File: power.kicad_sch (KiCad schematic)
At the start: 30 parts, among them Q2 BSS138-7-F, Q3 BSS138-7-F, Q7 SQS401EN-T1_BE3, U1 TPS56C230

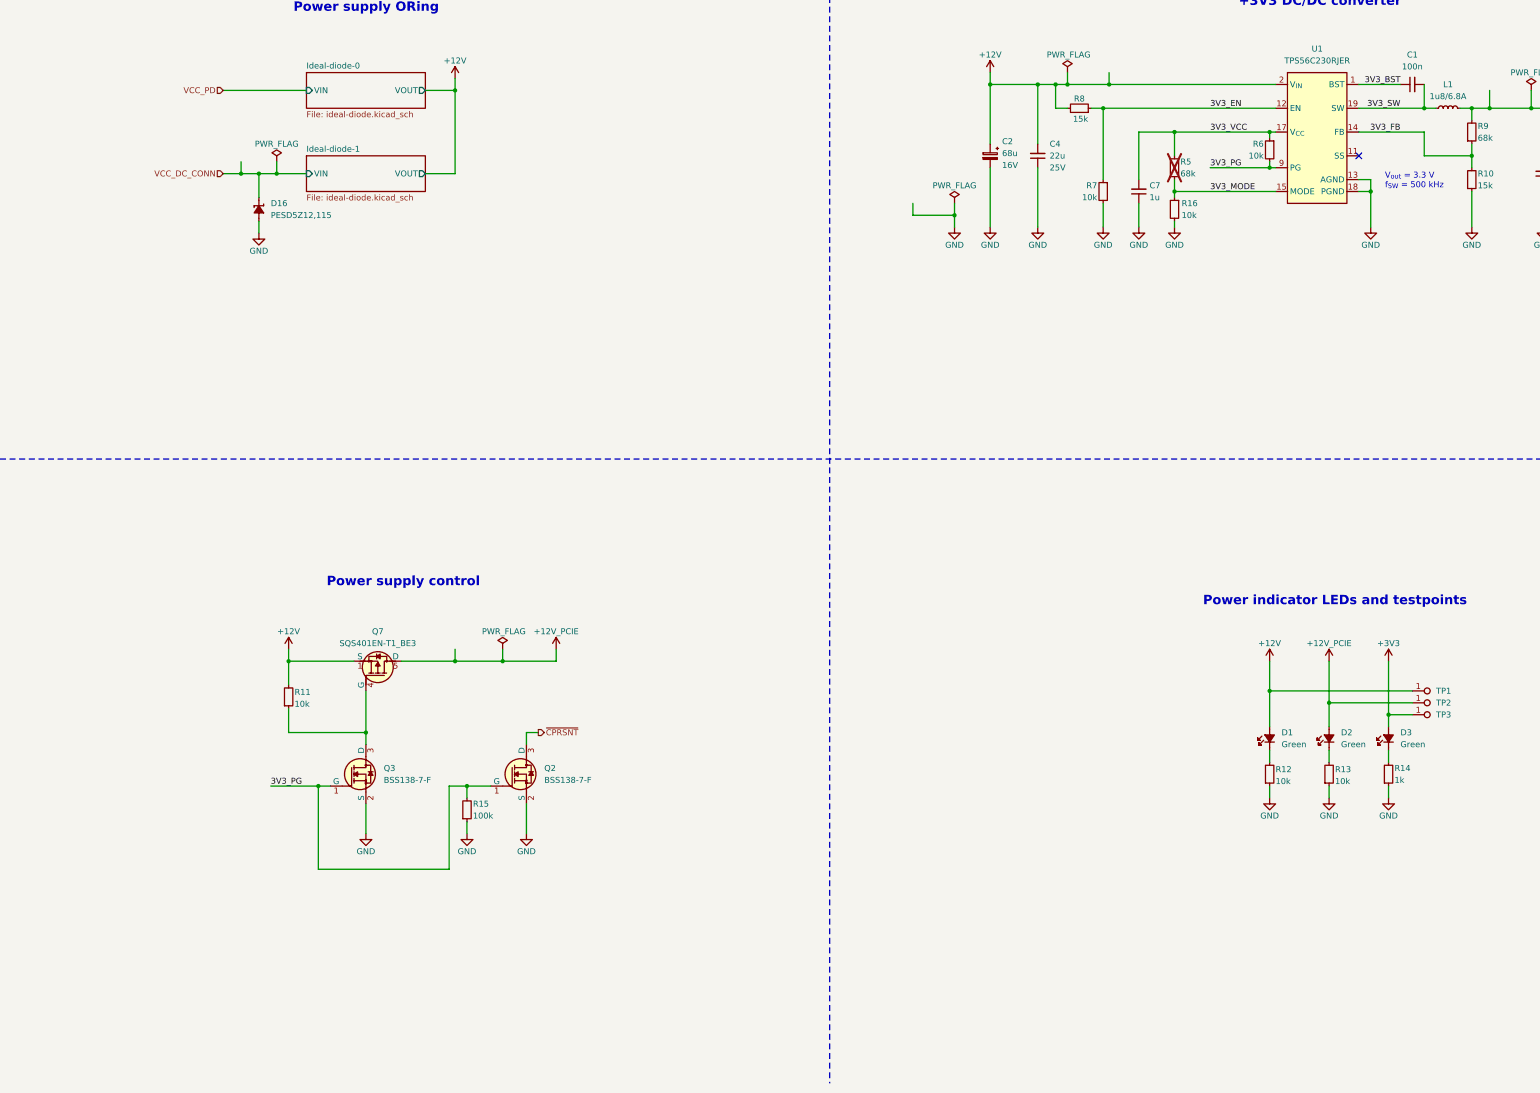
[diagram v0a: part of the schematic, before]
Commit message: [#79426] Removed power sequencing, added PERST control
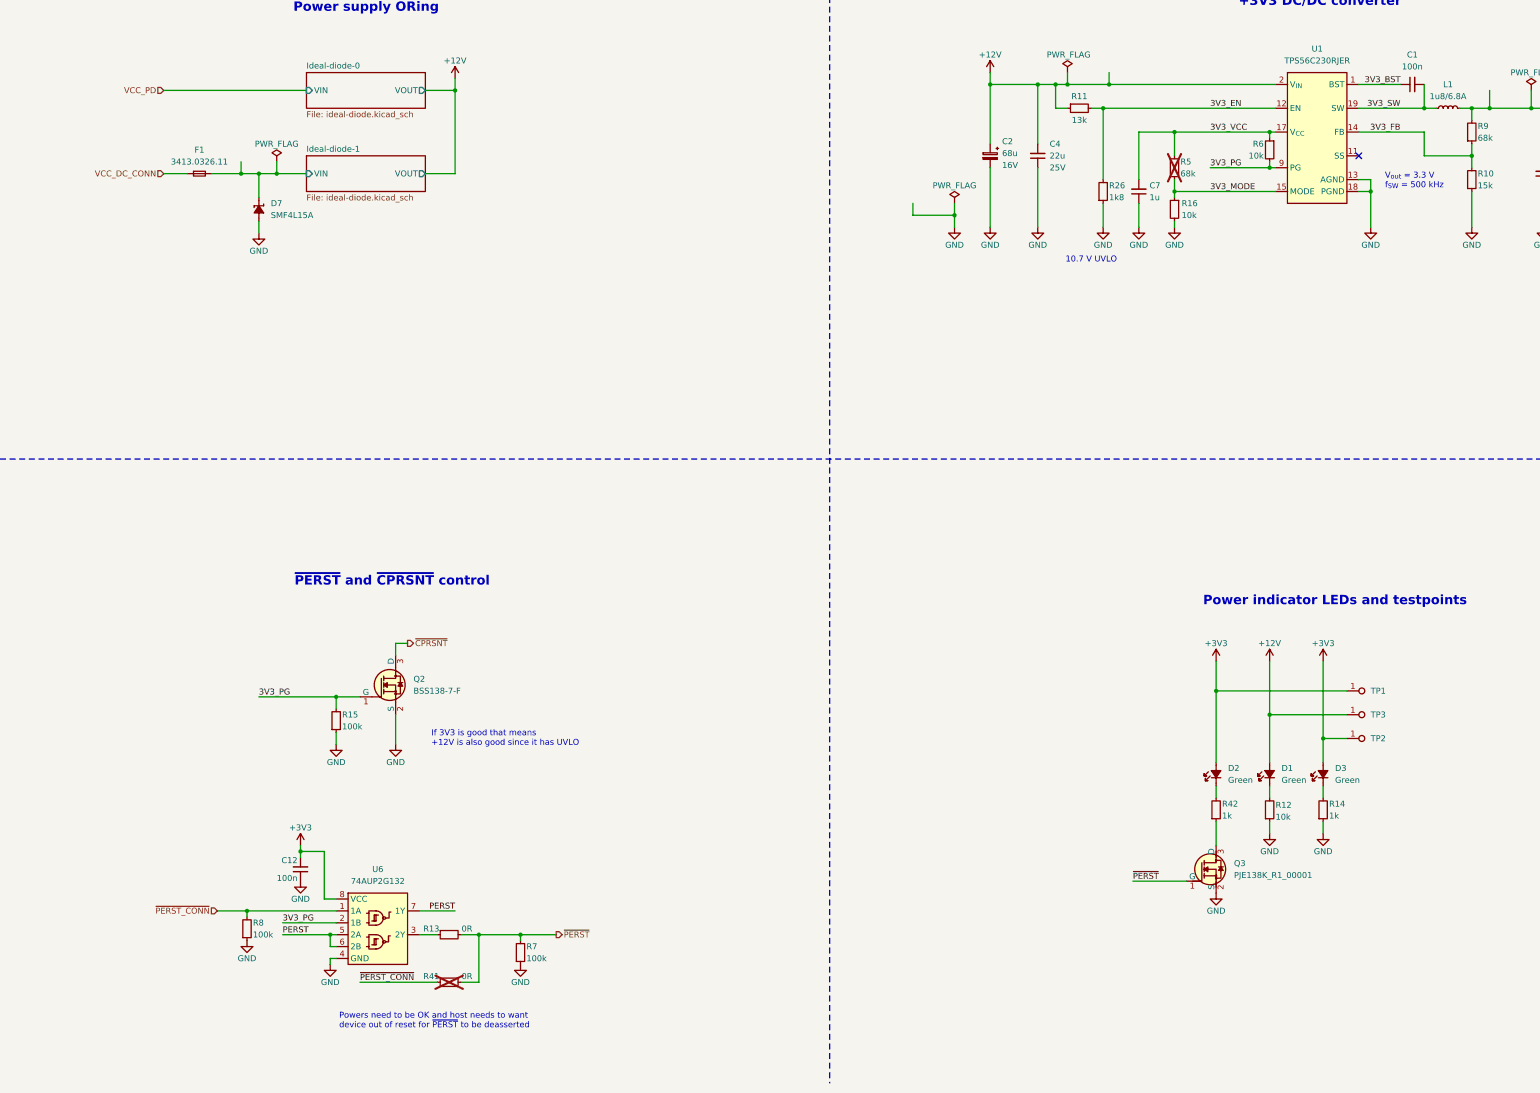
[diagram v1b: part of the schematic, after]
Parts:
- removed D16: PESD5Z12, antmicro-footprints:SOD-523, symbol antmicroTVSDiodes:PESD5Z12
- removed Q3: BSS138-7-F, antmicro-footprints:SOT-23-3, symbol antmicroTransistorsFETsMOSFETsSingle:BSS138-7-F
- removed Q7: SQS401EN-T1_BE3, antmicro-footprints:Vishay_PowerPAK_1212-8_Single, symbol antmicroTransistorsFETsMOSFETsSingle:SQS401EN-T1_BE3
- removed R11, R13, R7: R_10k_0402, antmicro-footprints:R_0402_1005Metric, symbol antmicroResistors0402:R_10k_0402
- removed R8: R_15k_0402, antmicro-footprints:R_0402_1005Metric, symbol antmicroResistors0402:R_15k_0402
- added C12: C_100n_0402, antmicro-footprints:C_0402_1005Metric, symbol antmicroCapacitors0402:C_100n_0402
- added D7: SMF4L15A, antmicro-footprints:SOD-123FL, symbol antmicroTVSDiodes:SMF4L15A
- added F1: F_7A_1206, antmicro-footprints:F_1206_3216Metric, symbol antmicroFuses:F_7A_1206
- added Q3: PJE138K, antmicro-footprints:SOT-523, symbol antmicroTransistorsFETsMOSFETsSingle:PJE138K
- added R11: R_13k_0402, antmicro-footprints:R_0402_1005Metric, symbol antmicroResistors0402:R_13k_0402
- added R13, R41: R_0R_0402, antmicro-footprints:R_0402_1005Metric, symbol antmicroResistors0402:R_0R_0402
- added R26: R_1k8_0603, antmicro-footprints:R_0603_1608Metric, symbol antmicroResistors0603:R_1k8_0603
- added R42: R_1k_0402, antmicro-footprints:R_0402_1005Metric, symbol antmicroResistors0402:R_1k_0402
- added R7, R8: R_100k_0402, antmicro-footprints:R_0402_1005Metric, symbol antmicroResistors0402:R_100k_0402
- added U6: 74AUP2G132, antmicro-footprints:VSSOP-8_2.3x2mm_P0.5mm, symbol antmicroLogicGatesandInverters:74AUP2G132
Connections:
- net +12V_PCIE is gone; now on net +3V3: D2.2 (A), TP2.1
- net +12V: now also TP3.1, R11.1; no longer TP1.1
- net +3V3: now also TP1.1, C12.2, U6.8 (VCC); no longer TP3.1
- net 3V3_EN: now also R11.2, R26.2
- net 3V3_PG: now also U6.2 (1B)
- net GND: now also C12.1, D7.2 (A), Q3.2 (S), R26.1, R7.1, R8.1, U6.4 (GND)
- net VCC_DC_CONN: now also F1.1
- net at D2.1 (C): now also R42.2
- new net: Q3.3 (D), R42.1
- new net: R13.1, U6.3 (2Y)
- new net Ideal-diode-1/VIN: D7.1 (C), F1.2
- new net PERST: U6.5 (2A), U6.6 (2B), U6.7 (1Y)
- new net ~{PERST_CONN}: R41.1, R8.2, U6.1 (1A)
- new net ~{PERST}: Q3.1 (G), R13.2, R41.2, R7.2
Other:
- note added: "10.7 V UVLO"
- note added: "If 3V3 is good that means +12V is also good since it has UVLO"
- note added: "Powers need to be OK and host needs to want device out of reset for ~{PERST} to be deasserted"
- note added: "~{PERST} and ~{CPRSNT} control"
- note removed: "Power supply control"
- moved on the sheet: D1, D3, Q2, R12, R14, R15, TP1, TP3

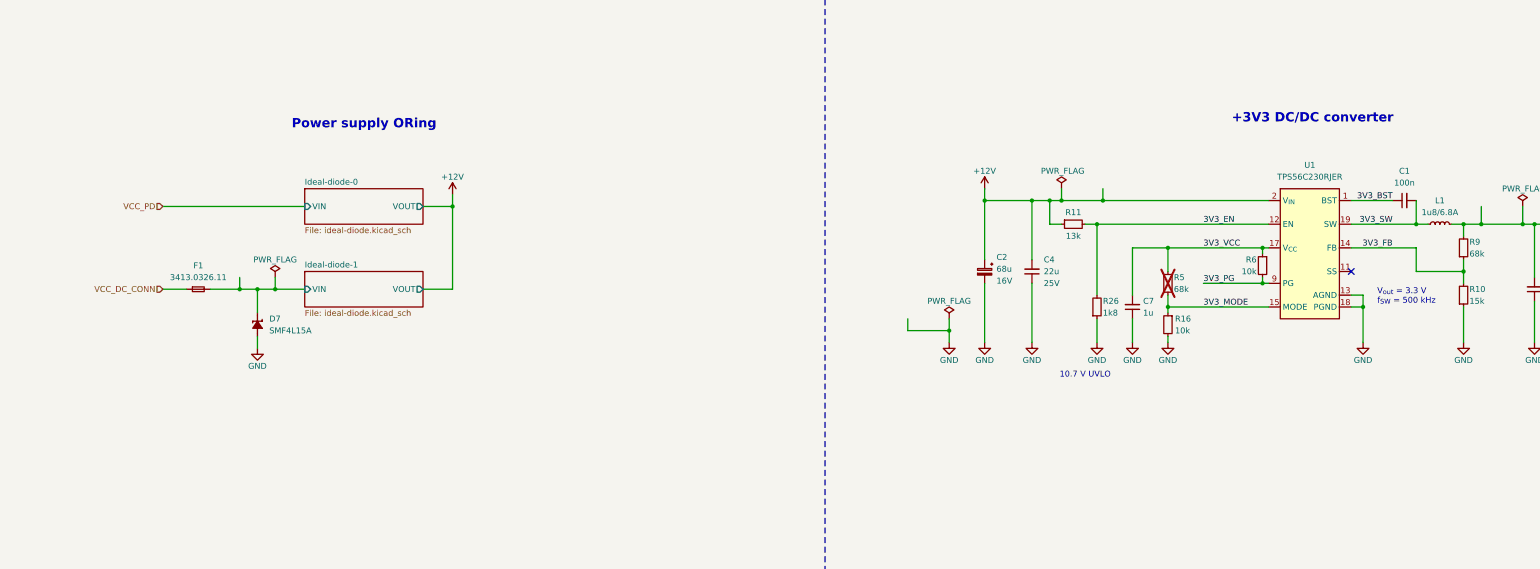
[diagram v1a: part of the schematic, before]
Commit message: [#79426] Connect DC input connectors via ideal diodes, change 15V TVS to 12V TVS
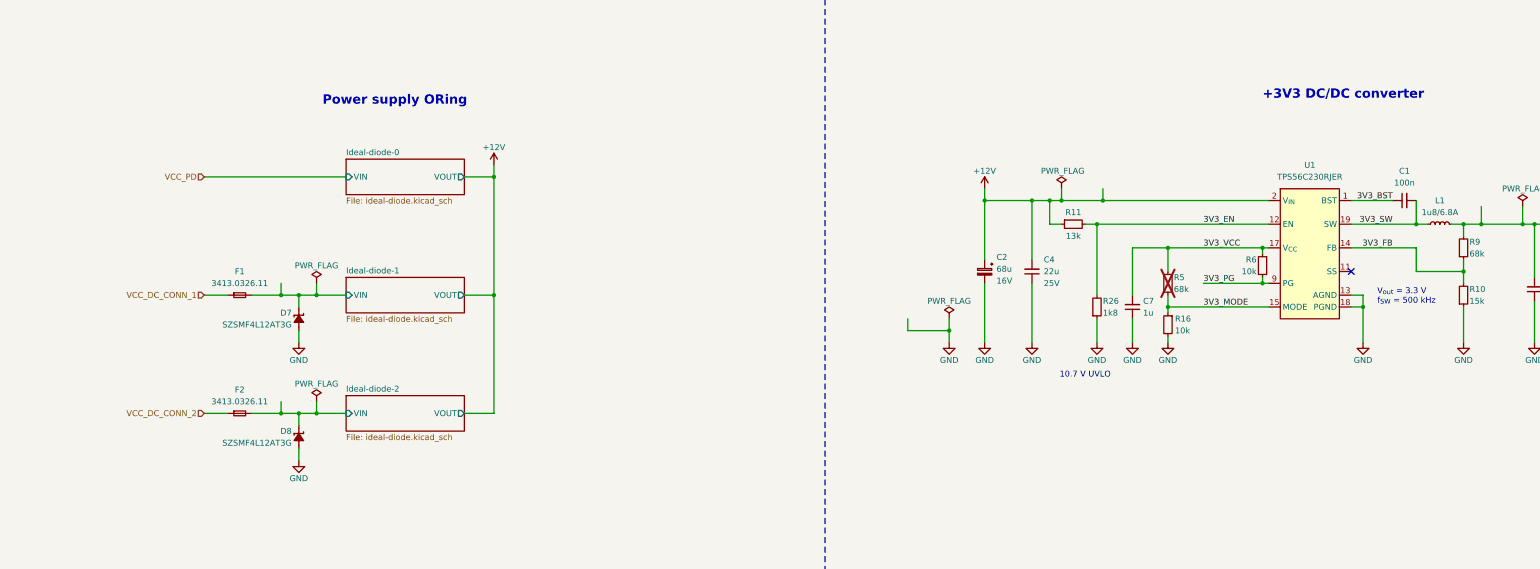
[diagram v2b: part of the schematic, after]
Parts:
- removed D7: SMF4L15A, antmicro-footprints:SOD-123FL, symbol antmicroTVSDiodes:SMF4L15A
- added D7, D8: SZSMF4L14AT3G, antmicro-footprints:SOD-123FL, symbol antmicroTVSDiodes:SZSMF4L14AT3G
- added F2: F_7A_1206, antmicro-footprints:F_1206_3216Metric, symbol antmicroFuses:F_7A_1206
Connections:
- net GND: now also D7.2 (A), D8.2 (A)
- net Ideal-diode-1/VIN: now also D7.1 (C)
- net VCC_DC_CONN renamed VCC_DC_CONN_1
- new net Ideal-diode-2/VIN: D8.1 (C), F2.2
- new net VCC_DC_CONN_2: F2.1
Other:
- added sheet Ideal-diode-2 (ideal-diode.kicad_sch)
- moved on the sheet: F1

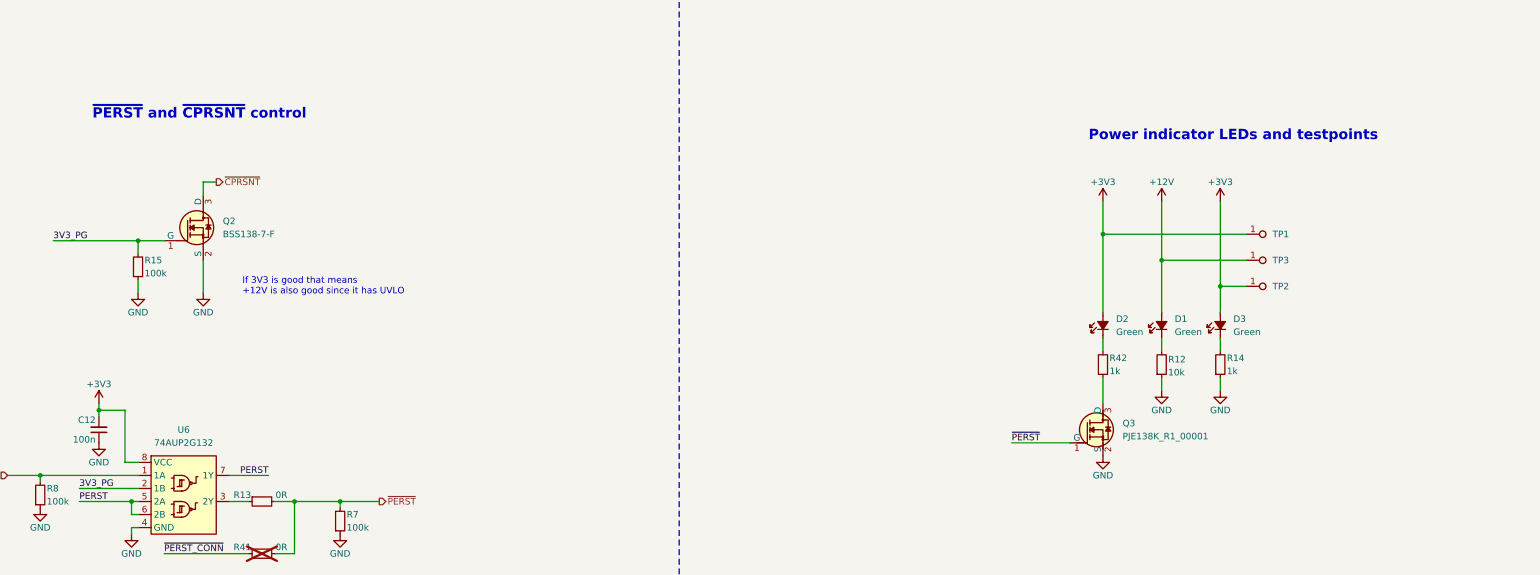
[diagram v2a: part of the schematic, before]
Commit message: [#79426] Change Q3 MOSFET
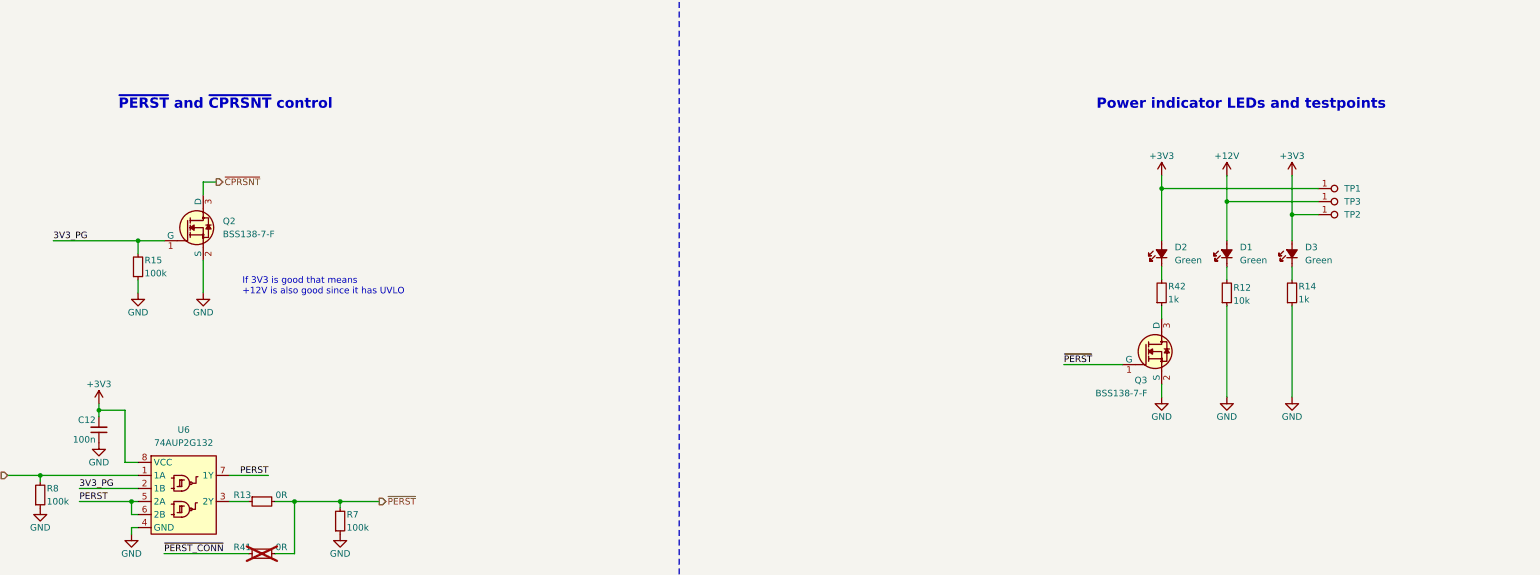
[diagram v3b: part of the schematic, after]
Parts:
- removed Q3: PJE138K, antmicro-footprints:SOT-523, symbol antmicroTransistorsFETsMOSFETsSingle:PJE138K
- added Q3: BSS138-7-F, antmicro-footprints:SOT-23-3, symbol antmicroTransistorsFETsMOSFETsSingle:BSS138-7-F
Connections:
- net GND: now also Q3.2 (S)
- net ~{PERST}: now also Q3.1 (G)
- net at R42.1: now also Q3.3 (D)
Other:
- moved on the sheet: D1, D2, D3, R12, R14, R42, TP1, TP2, TP3

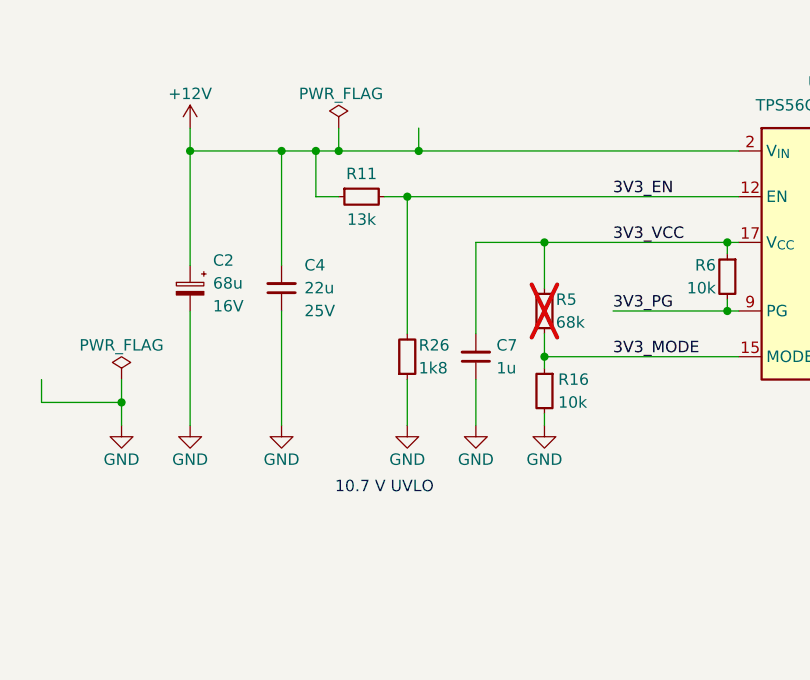
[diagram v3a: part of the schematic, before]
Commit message: [#79426] Change 3V3 DC-DC UVLO to 11.3V
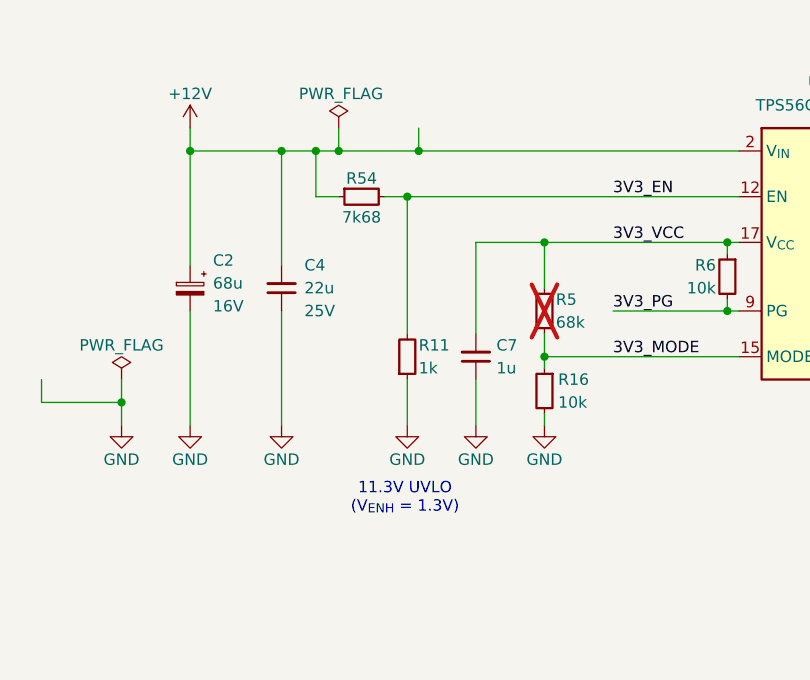
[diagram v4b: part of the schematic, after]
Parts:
- removed R11: R_13k_0402, antmicro-footprints:R_0402_1005Metric, symbol antmicroResistors0402:R_13k_0402
- removed R26: R_1k8_0603, antmicro-footprints:R_0603_1608Metric, symbol antmicroResistors0603:R_1k8_0603
- added R11: R_1k_0402, antmicro-footprints:R_0402_1005Metric, symbol antmicroResistors0402:R_1k_0402
- added R54: R_7k68_0402, antmicro-footprints:R_0402_1005Metric, symbol antmicroResistors0402:R_7k68_0402
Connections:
- net +12V: now also R54.1
- net 3V3_EN: now also R11.2, R54.2
- net GND: now also R11.1
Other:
- note added: "11.3V UVLO (V_{ENH} = 1.3V)"
- note removed: "10.7 V UVLO"
